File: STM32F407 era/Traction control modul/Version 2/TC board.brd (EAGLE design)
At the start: 134.6 x 100 mm, 90 parts, among them IC1 74HC14D, IC2 lm2575, IC3 74AC08D, IC5 REG1117, IC6 74AC14D, J1 CON1, J2 CON1, Q5 IRFR3707ZR, Q8 IRFR3707ZR, U1 MAX13052ESA+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

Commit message: more work on h-bridge layout
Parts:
- removed X3: (no value), con-wago-500:W237-103
- added X5: 5566-10, con-molex:5566-10
- moved J2 14.9 mm to (121.9, 91.1), turned to 0 degrees
- moved X2 6.55 mm to (97.8, 54.9)
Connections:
- removed net N$27: U$28.1, U$28.25, U$28.30, U$28.SLUG3, X3.1
- removed net N$37: U$28.15, U$28.16, U$28.21, U$28.SLUG2, X3.2
- new net OUTA: U$28.1, U$28.25, U$28.30, U$28.SLUG3, X5.1, X5.6
- new net OUTB: U$28.15, U$28.16, U$28.21, U$28.SLUG2, X5.2, X5.7
- net MP: now also X5.3; no longer X3.3
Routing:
- net N$37: track 58.2 -> 0.00 mm, vias 2 -> 0
- net N$27: track 57.9 -> 0.00 mm
- net N$53: track 74.5 -> 34.3 mm
- net MP: track 34.1 -> 0.00 mm, vias 3 -> 0
- net GNDS: track 44.8 -> 14.3 mm, vias 12 -> 3
- added copper zone on layer 1, net OUTA
- added copper zone on layer 16, net OUTA
- added copper zone on layer 1, net OUTB
- added copper zone on layer 16, net OUTB
- removed copper zone on layer 1, net GNDS

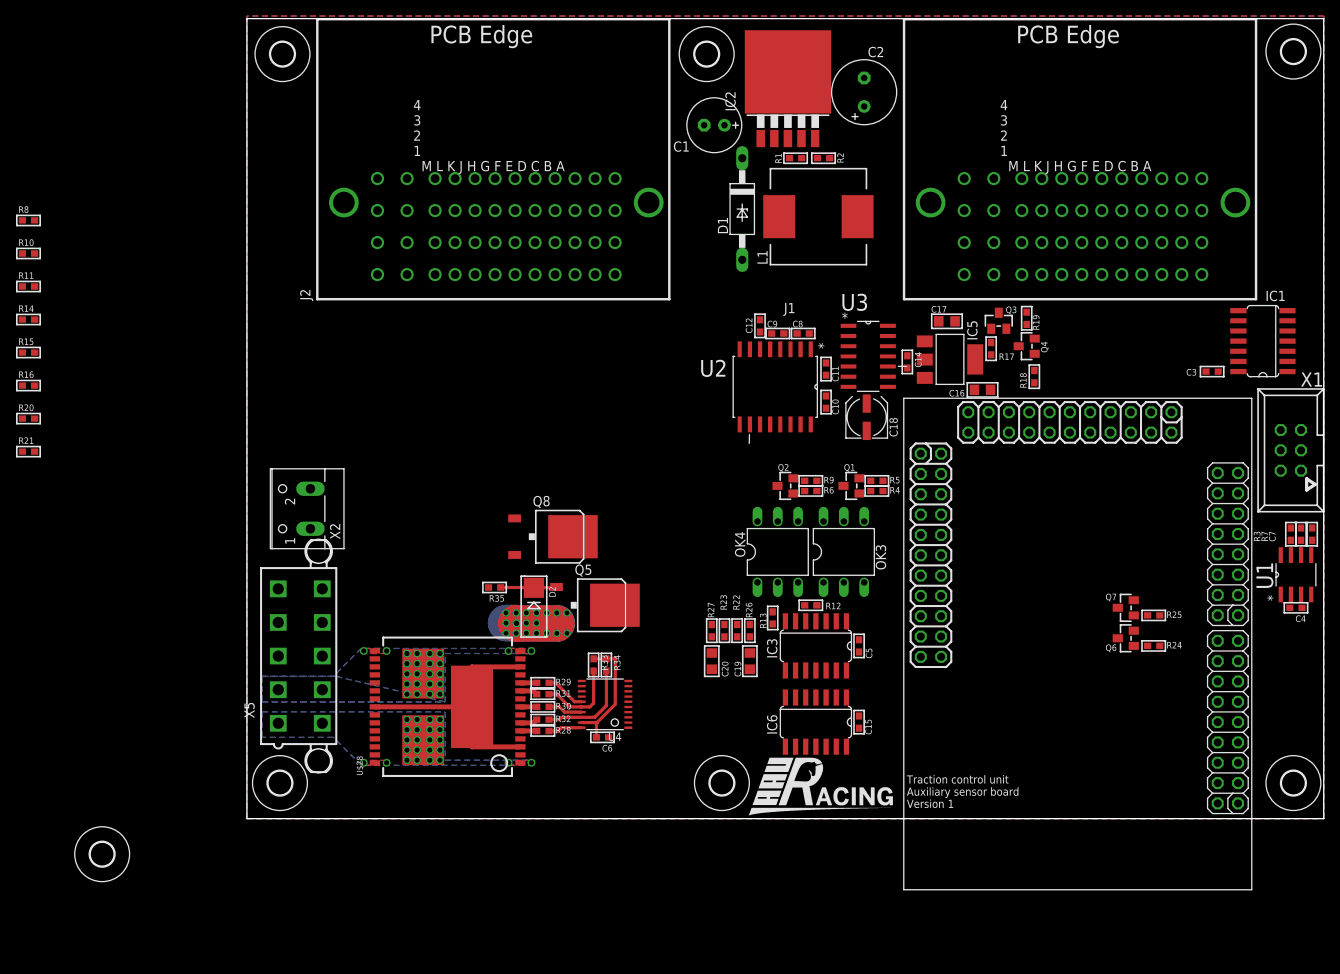
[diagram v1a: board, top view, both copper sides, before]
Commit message: more work on TC, first layout of 3G test board
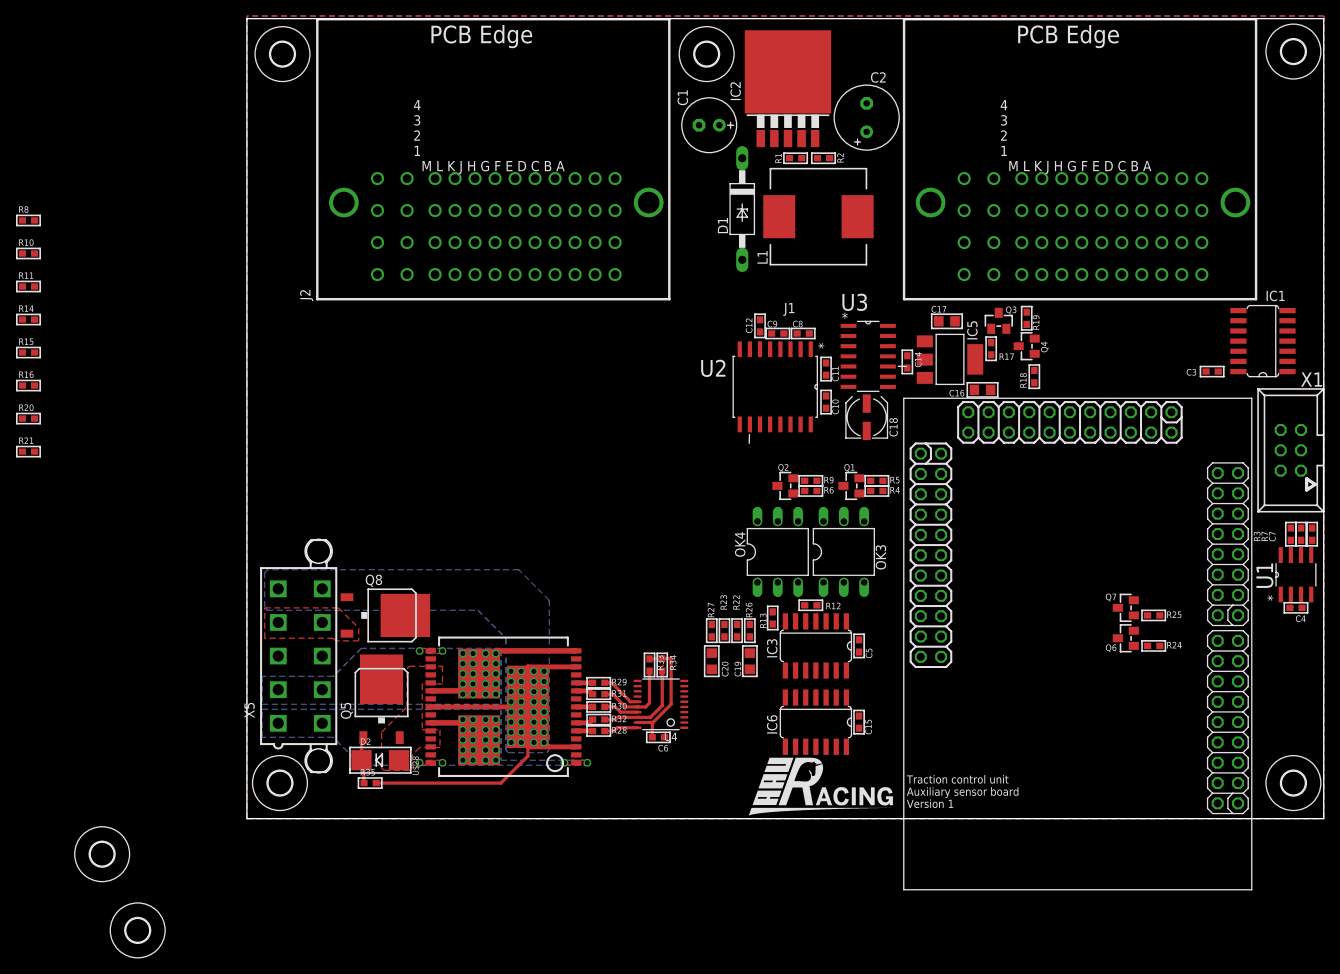
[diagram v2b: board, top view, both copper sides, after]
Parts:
- removed X2: (no value), con-wago-500:W237-102
- moved H3 75.3 mm to (77.5, 2.22)
- moved Q5 29.1 mm to (108.0, 31.1), turned to 0 degrees
- moved R35 29.0 mm to (106.5, 20.6), turned to 0 degrees
- moved D2 27.2 mm to (107.8, 23.5), turned to 0 degrees
- moved Q8 23.2 mm to (108.4, 41.6)
- moved C6 6.99 mm to (142.6, 26.4)
- moved U4 6.99 mm to (142.9, 30.5)
- moved U$28 6.98 mm to (123.2, 30.2)
- moved R28 6.98 mm to (135.1, 27.1)
- moved R29 6.98 mm to (135.1, 33.2)
- moved R30 6.98 mm to (135.1, 30.2)
- moved R31 6.98 mm to (135.1, 31.8)
- moved R32 6.98 mm to (135.1, 28.6)
- moved R33 6.98 mm to (141.4, 35.4)
- moved R34 6.98 mm to (143.0, 35.4)
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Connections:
- net OUTB renamed CVVM
- removed net MP: Q8.3, X5.3
- removed net N$53: R35.2, U$28.13, U$28.23, U$28.3, U$28.SLUG1, X2.1
- new net GNDM: Q8.3, X5.4, X5.9
- new net VCCM: R35.2, U$28.13, U$28.23, U$28.3, U$28.SLUG1, X5.10, X5.5
- net GND: now also X5.3, X5.8; no longer X2.2
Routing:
- net VCCM: track 0.00 -> 57.1 mm, vias 0 -> 32
- net N$53: track 34.3 -> 0.00 mm
- net CVVM: track 0.00 -> 16.9 mm, vias 24 -> 22
- net GNDS: track 14.3 -> 0.00 mm, vias 3 -> 0
- net OUTA: track 0.00 -> 6.50 mm
- net N$45: track 7.03 -> 6.29 mm
- added copper zone on layer 1, net GNDM
- added copper zone on layer 1, net GNDS
- added copper zone on layer 16, net VCCM
